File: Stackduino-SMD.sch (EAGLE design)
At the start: 49 parts

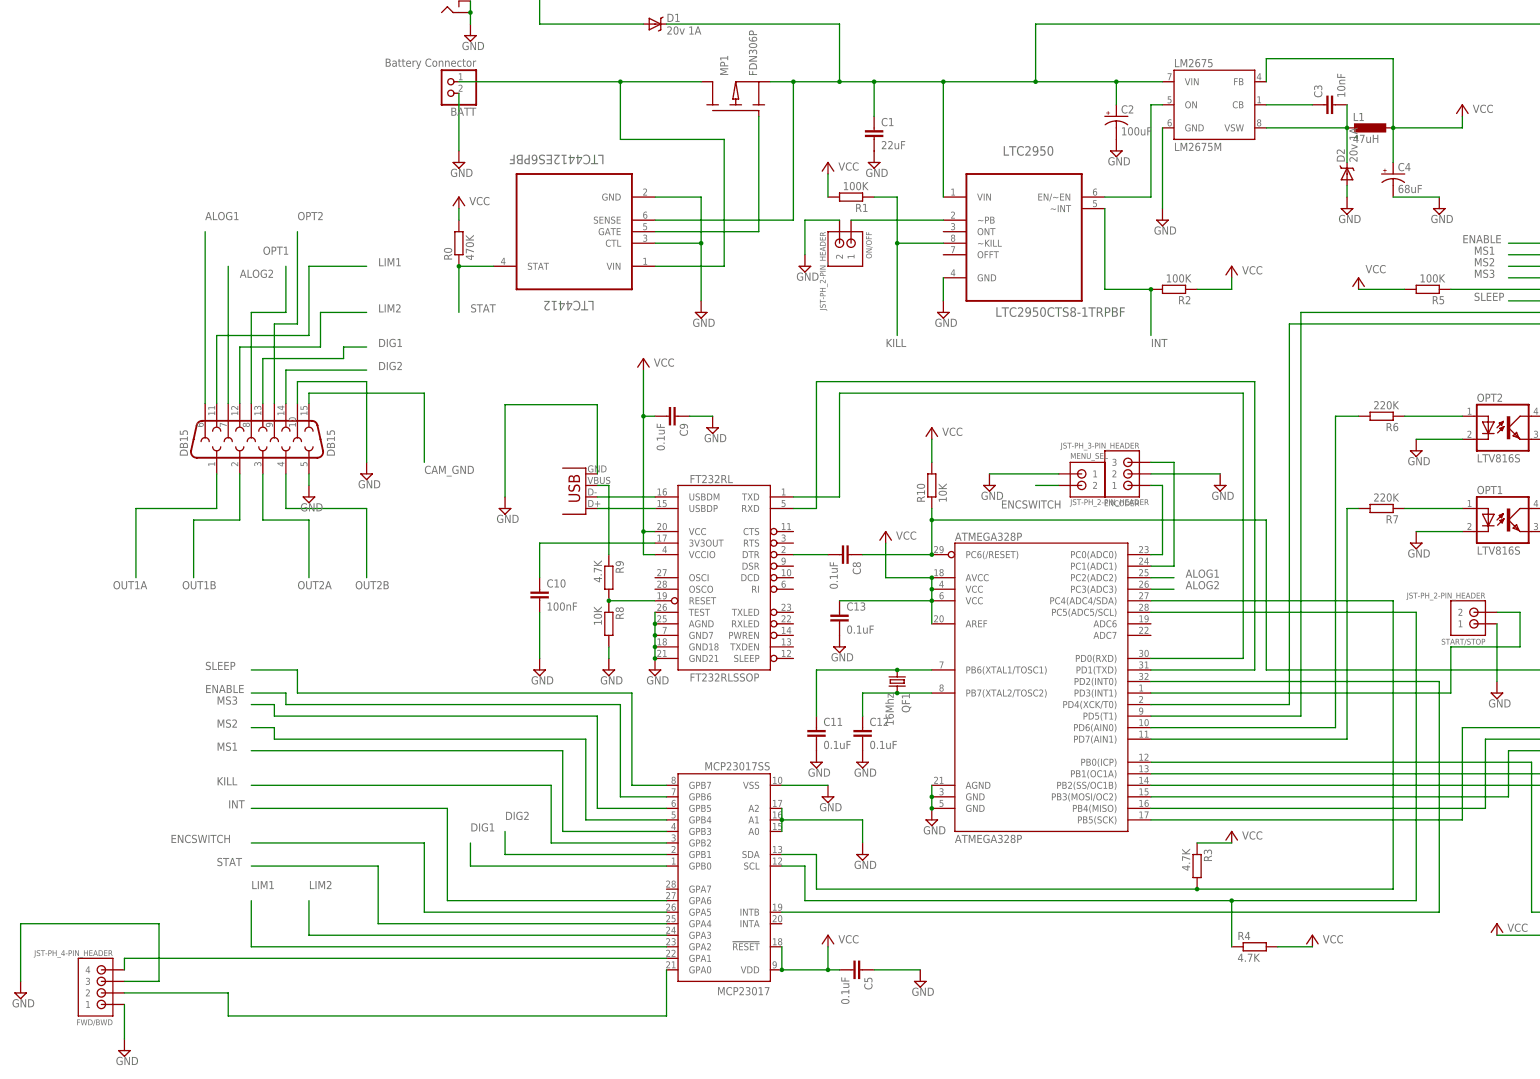
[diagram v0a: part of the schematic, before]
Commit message: Amended cap values on crystal
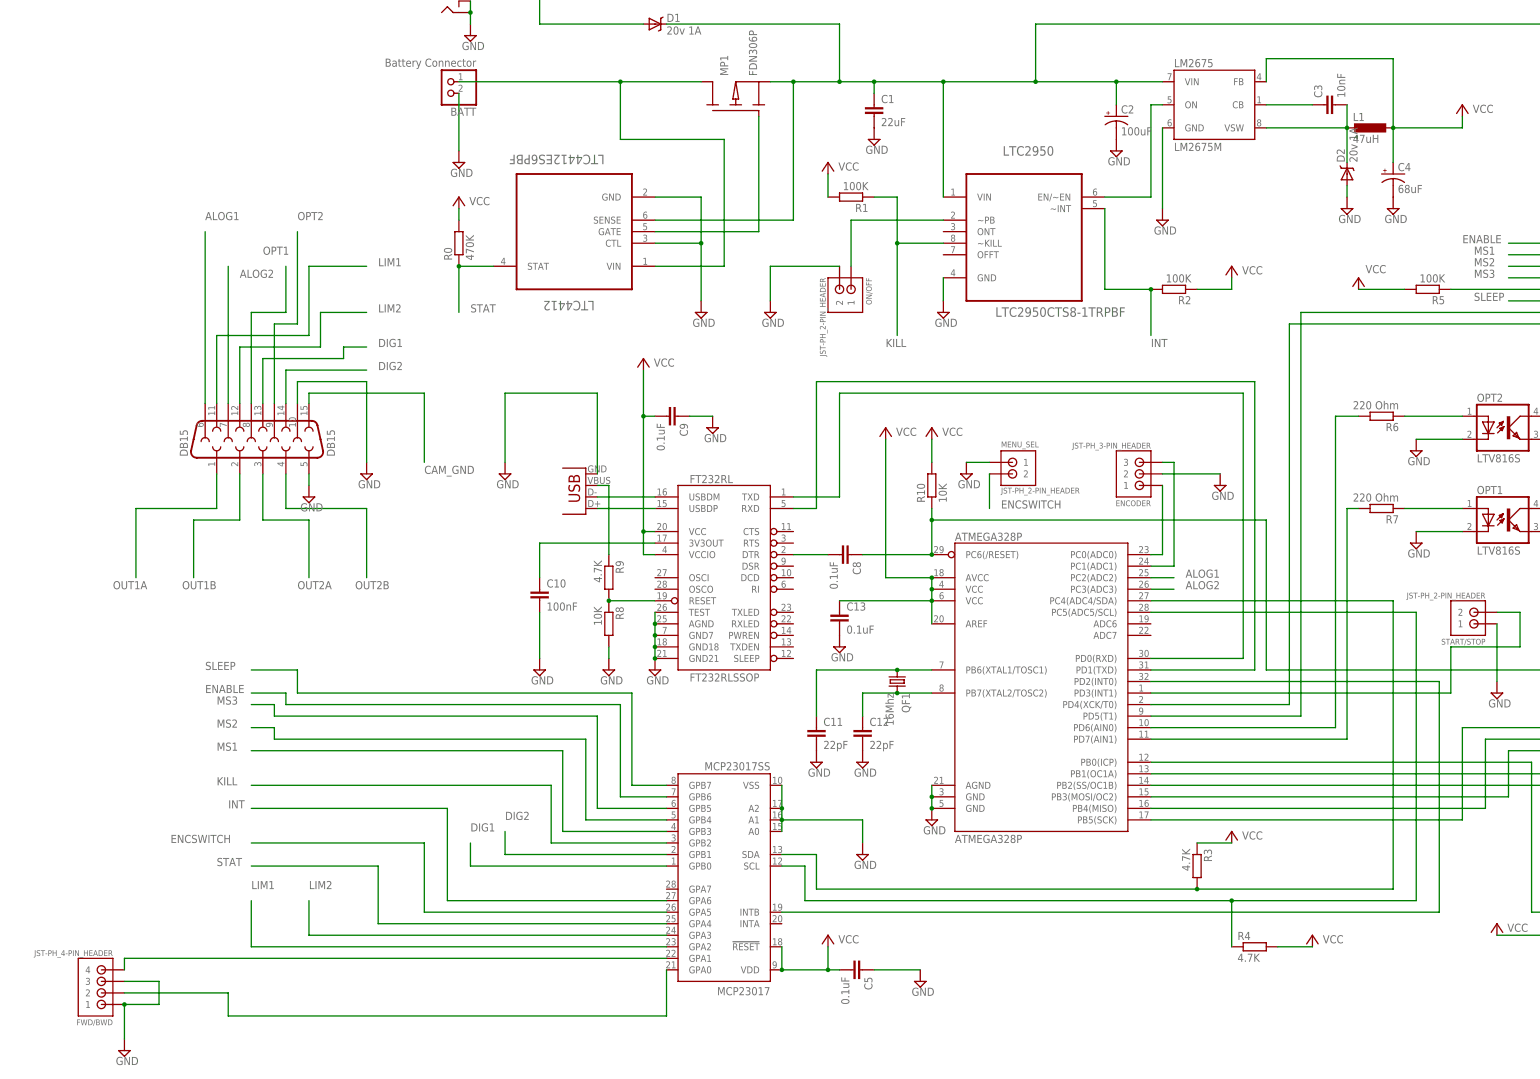
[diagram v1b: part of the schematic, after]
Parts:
- C11, C12: value 0.1uF -> 22pF
- R6, R7: value 220K -> 220 Ohm
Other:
- moved on the sheet: C1, ENCODER, MENU_SEL, ON/OFF

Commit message: changes inc battery monitor
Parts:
- added ENCODER1: JST-PH_3-PIN_HEADER, SRG:JST-PH_3-PIN_HEADER
- added MENU_SEL1: JST-PH_2-PIN_HEADER, SRG:JST-PH_2-PIN_HEADER
- added MP2, MP3: NOT SURE YET, sym:PMOS
- added R11, R12, R14: 10K, eagle-ltspice:R
- added R13: 150 Ohm, eagle-ltspice:R
- added R15: 4.7K, eagle-ltspice:R
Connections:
- net N$10 renamed GATE
- net VDD renamed BATTVIN
- new net BATT_FET: ATMEGA328P.PC3(ADC3), R13.1
- new net BATT_SENSE: ATMEGA328P.PC2(ADC2), R14.1, R15.2
- new net BATT_VOLT: MP3.D
- new net EXTRA_INPUT: MCP23017.GPA7, MENU_SEL1.1
- new net N$12: MP3.G, R13.2
- new net N$16: MP3.S, R14.2
- new net N$8: MCP23017.!RESET, R12.1
- new net N$9: A4988_CARRIER.VMOT, MP2.S
- net ALOG1: now also ATMEGA328P.ADC6; no longer ATMEGA328P.PC2(ADC2)
- net ALOG2: now also ATMEGA328P.ADC7; no longer ATMEGA328P.PC3(ADC3)
- net ENCSWITCH: now also MENU_SEL.1; no longer MENU_SEL.2
- net GND: now also MENU_SEL.2, MENU_SEL1.2, R15.1; no longer MENU_SEL.1
- net PBUTTON: now also R11.1
- net V+: now also MP2.D, R11.2; no longer A4988_CARRIER.VMOT
- net VCC: now also MP2.G, R12.2; no longer MCP23017.!RESET
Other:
- moved on the sheet: C5, FWD/BWD

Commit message: latest progress
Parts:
- removed BATT: Battery Connector, adafruit:JST_2PIN-THM-RA
- removed ENCODER1: JST-PH_3-PIN_HEADER, SRG:JST-PH_3-PIN_HEADER
- added BATT_IN: JST-PH_3-PIN_HEADER, SRG:JST-PH_3-PIN_HEADER
- added R16: 10K, eagle-ltspice:R
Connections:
- new net N$10: BATT_IN.1
- net BATTVIN: now also BATT_IN.2; no longer BATT.2
- net GND: now also BATT_IN.3, R16.1; no longer BATT.1
- net N$12: now also R16.2
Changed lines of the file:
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@@
 <setting verticaltext="up"/>
 </settings>
-<grid distance="0.1" unitdist="inch" unit="inch" style="lines" multiple="1" display="yes" altdistance="0.01" altunitdist="inch" altunit="inch"/>
+<grid distance="0.1" unitdist="inch" unit="inch" style="lines" multiple="1" display="no" altdistance="0.01" altunitdist="inch" altunit="inch"/>
 <layers>
 <layer number="1" name="Top" color="4" fill="1" visible="no" active="no"/>
@@
 <part name="SUPPLY14" library="supply2" deviceset="GND" device=""/>
 <part name="SUPPLY15" library="supply2" deviceset="GND" device=""/>
-<part name="BATT" library="adafruit" deviceset="JST_2PIN" device="-THM-RA" value="Battery Connector"/>
 <part name="C8" library="eagle-ltspice" deviceset="C" device="" value="0.1uF"/>
 <part name="R10" library="eagle-ltspice" deviceset="R" device="" value="10K"/>
@@
 <part name="R11" library="eagle-ltspice" deviceset="R" device="" value="10K"/>
 <part name="R12" library="eagle-ltspice" deviceset="R" device="" value="10K"/>
-<part name="ENCODER1" library="SRG" deviceset="JST-PH_3-PIN_HEADER" device=""/>
+<part name="BATT_IN" library="SRG" deviceset="JST-PH_3-PIN_HEADER" device=""/>
 <part name="MP2" library="sym" deviceset="PMOS" device="" value="NOT SURE YET"/>
 <part name="P+5" library="supply1" deviceset="+5V" device="" value="VCC"/>
@@
 <part name="MENU_SEL1" library="SRG" deviceset="JST-PH_2-PIN_HEADER" device=""/>
 <part name="SUPPLY18" library="supply2" deviceset="GND" device=""/>
+<part name="R16" library="eagle-ltspice" deviceset="R" device="" value="10K"/>
+<part name="SUPPLY13" library="supply2" deviceset="GND" device=""/>
 </parts>
 <sheets>
@@
 <instance part="SUPPLY7" gate="GND" x="-45.72" y="63.5"/>
 <instance part="SUPPLY8" gate="GND" x="-99.06" y="63.5"/>
-<instance part="SUPPLY9" gate="GND" x="-152.4" y="96.52"/>
+<instance part="SUPPLY9" gate="GND" x="-152.4" y="104.14"/>
 <instance part="D1" gate="G$1" x="-109.22" y="127"/>
 <instance part="MP1" gate="G$1" x="-99.06" y="106.68" rot="R90"/>
@@
 <instance part="SUPPLY14" gate="GND" x="-109.22" y="-15.24"/>
 <instance part="SUPPLY15" gate="GND" x="-142.24" y="27.94"/>
-<instance part="BATT" gate="G$1" x="-154.94" y="114.3" rot="R180"/>
 <instance part="C8" gate="G$1" x="-66.04" y="10.16" rot="R270"/>
 <instance part="R10" gate="G$1" x="-48.26" y="25.4" rot="R90"/>
@@
 <instance part="R11" gate="G$1" x="-50.8" y="96.52" rot="R90"/>
 <instance part="R12" gate="G$1" x="-73.66" y="-76.2"/>
-<instance part="ENCODER1" gate="G$1" x="-165.1" y="106.68" rot="R180"/>
+<instance part="BATT_IN" gate="G$1" x="-182.88" y="114.3" rot="R180"/>
 <instance part="MP2" gate="G$1" x="132.08" y="96.52" rot="R90"/>
 <instance part="P+5" gate="1" x="91.44" y="104.14" smashed="yes">
@@
 <instance part="MENU_SEL1" gate="G$1" x="142.24" y="22.86"/>
 <instance part="SUPPLY18" gate="GND" x="134.62" y="12.7"/>
+<instance part="R16" gate="G$1" x="-241.3" y="-50.8" rot="R180"/>
+<instance part="SUPPLY13" gate="GND" x="-226.06" y="-53.34"/>
 </instances>
 <busses>
@@
 </segment>
 <segment>
-<pinref part="BATT" gate="G$1" pin="1"/>
 <pinref part="SUPPLY9" gate="GND" pin="GND"/>
-<wire x1="-152.4" y1="111.76" x2="-152.4" y2="99.06" width="0.1524" layer="91"/>
+<wire x1="-152.4" y1="116.84" x2="-152.4" y2="106.68" width="0.1524" layer="91"/>
+<pinref part="BATT_IN" gate="G$1" pin="3"/>
+<wire x1="-177.8" y1="116.84" x2="-152.4" y2="116.84" width="0.1524" layer="91"/>
 </segment>
 <segment>
@@
 <wire x1="134.62" y1="15.24" x2="134.62" y2="22.86" width="0.1524" layer="91"/>
 </segment>
+<segment>
+<pinref part="R16" gate="G$1" pin="1"/>
+<wire x1="-236.22" y1="-50.8" x2="-226.06" y2="-50.8" width="0.1524" layer="91"/>
+<pinref part="SUPPLY13" gate="GND" pin="GND"/>
+</segment>
 </net>
 <net name="PBUTTON" class="0">
@@
 <wire x1="-116.84" y1="101.6" x2="-116.84" y2="114.3" width="0.1524" layer="91"/>
 <pinref part="MP1" gate="G$1" pin="D"/>
-<pinref part="BATT" gate="G$1" pin="2"/>
-<wire x1="-152.4" y1="114.3" x2="-116.84" y2="114.3" width="0.1524" layer="91"/>
 <junction x="-116.84" y="114.3"/>
+<pinref part="BATT_IN" gate="G$1" pin="2"/>
+<wire x1="-177.8" y1="114.3" x2="-116.84" y2="114.3" width="0.1524" layer="91"/>
 </segment>
 </net>
@@
 <pinref part="R13" gate="G$1" pin="2"/>
 <wire x1="-256.54" y1="-40.64" x2="-251.46" y2="-40.64" width="0.1524" layer="91"/>
+<wire x1="-256.54" y1="-40.64" x2="-256.54" y2="-50.8" width="0.1524" layer="91"/>
+<junction x="-256.54" y="-40.64"/>
+<pinref part="R16" gate="G$1" pin="2"/>
+<wire x1="-256.54" y1="-50.8" x2="-246.38" y2="-50.8" width="0.1524" layer="91"/>
 </segment>
 </net>
@@
 </segment>
 </net>
+<net name="N$10" class="0">
+<segment>
+<pinref part="BATT_IN" gate="G$1" pin="1"/>
+<wire x1="-177.8" y1="111.76" x2="-172.72" y2="111.76" width="0.1524" layer="91"/>
+<wire x1="-172.72" y1="111.76" x2="-172.72" y2="104.14" width="0.1524" layer="91"/>
+</segment>
+</net>

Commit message: Battery monitor and VMOT Mosfets added
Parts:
- removed MENU_SEL1: JST-PH_2-PIN_HEADER, SRG:JST-PH_2-PIN_HEADER
- added DIG_INPUT: JST-PH_2-PIN_HEADER, SRG:JST-PH_2-PIN_HEADER
- MP2, MP3: value NOT SURE YET -> NTR4501N
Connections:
- net N$28 renamed START_STOP
- net N$33 renamed FWD
- net N$35 renamed BWD
- net PC0 renamed ENC_A
- net PC1 renamed ENC_B
- removed net N$10: BATT_IN.1
- net BATT_VOLT: now also BATT_IN.1
- net EXTRA_INPUT: now also DIG_INPUT.1; no longer MENU_SEL1.1
- net GND: now also DIG_INPUT.2; no longer MENU_SEL1.2
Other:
- note added: "1.1"
- note added: "https://github.com/ReallySmall/Stackduino-2"
- moved on the sheet: 12VDC, ATMEGA328P, BATT_IN, C1, C10, C11, C12, C13, C2, C3, C4, C5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
